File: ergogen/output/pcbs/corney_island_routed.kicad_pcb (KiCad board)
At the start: 2 copper layers, 134.2 x 92.7 mm, 67 parts

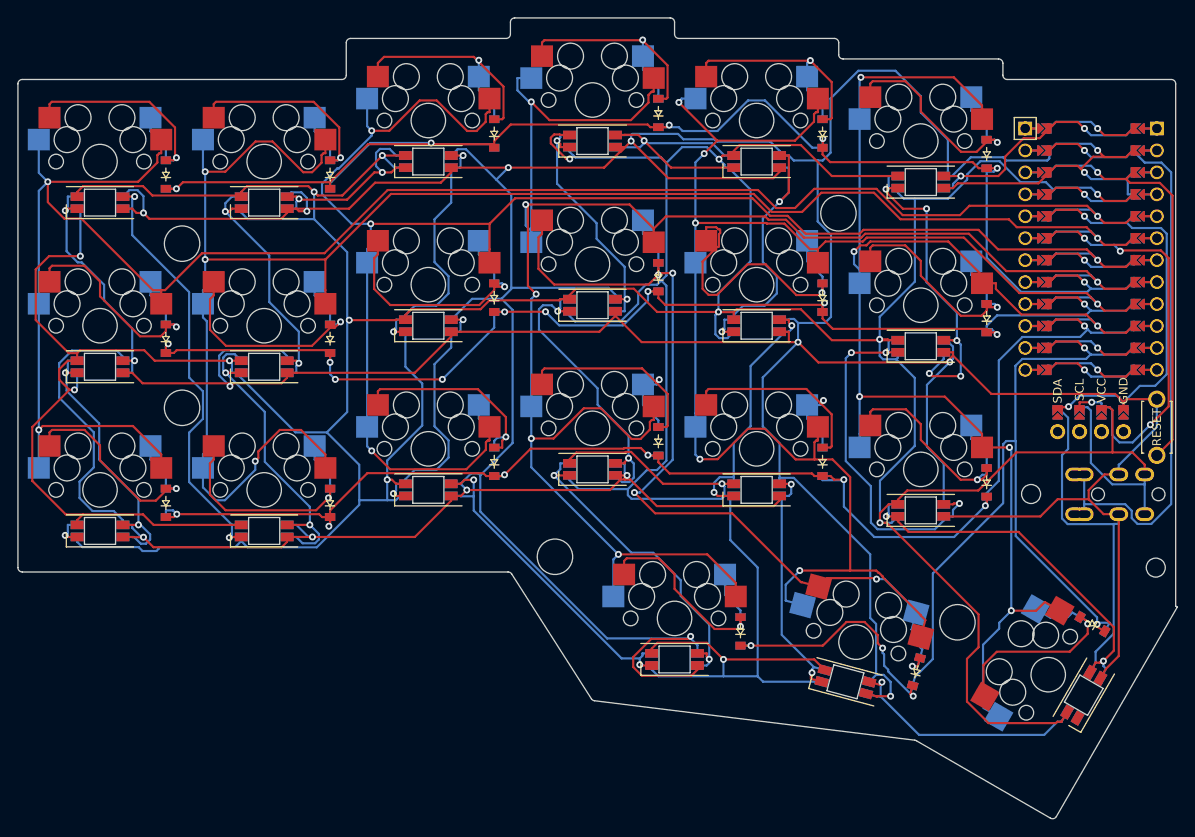
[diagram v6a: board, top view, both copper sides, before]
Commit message: Add underglow LEDs
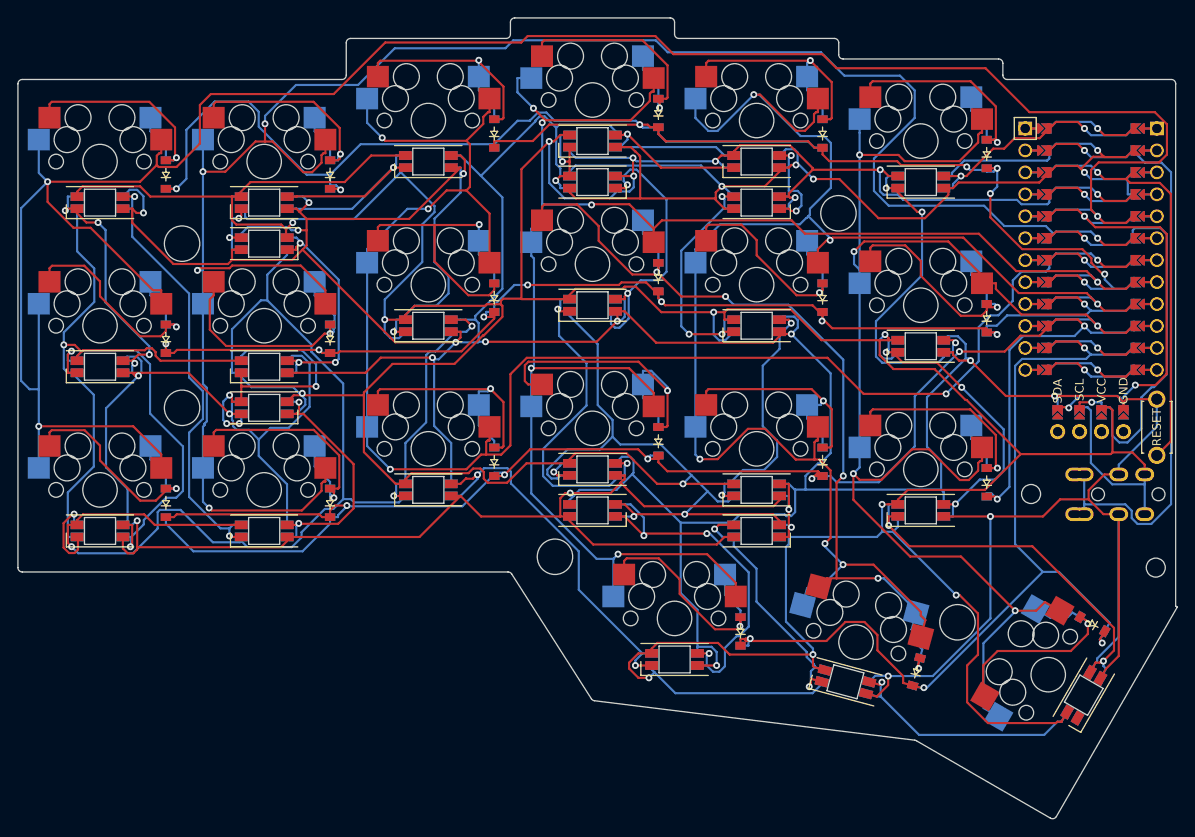
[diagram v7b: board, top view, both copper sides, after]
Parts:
- added LED23: YS-SK6812MINI-E, YS-SK6812MINI-E, F.Cu at (119.0, 71.5)
- added LED24: YS-SK6812MINI-E, YS-SK6812MINI-E, F.Cu at (157.0, 102.4)
- added LED25: YS-SK6812MINI-E, YS-SK6812MINI-E, F.Cu at (157.0, 64.4)
- added LED26: YS-SK6812MINI-E, YS-SK6812MINI-E, F.Cu at (176.0, 104.8)
- added LED27: YS-SK6812MINI-E, YS-SK6812MINI-E, F.Cu at (176.0, 66.8)
- added LED28: , combo_display, F.Cu at (214.6, 91.2)
- LED22: value combined_oled -> YS-SK6812MINI-E; footprint combined_oled -> YS-SK6812MINI-E
- moved LED22 95.6 mm to (119.0, 90.5)
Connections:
- LED10 pad 2: LED_11 -> ULED_3
- LED12 pad 2: LED_9 -> ULED_2
- LED13 pad 4: LED_5 -> ULED_5
- LED15 pad 4: LED_7 -> ULED_6
- LED22 pad 1: GND -> VCC
- LED22 pad 2: VCC -> LED_17
- LED22 pad 3: SCL -> GND
- LED22 pad 4: SDA -> ULED_0
- LED5 pad 2: LED_17 -> ULED_0
- LED6 pad 2: LED_16 -> ULED_1
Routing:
- net VCC: track 765.4 -> 879.6 mm, vias 15 -> 21
- net C0: track 222.1 -> 265.9 mm
- net R2: track 158.9 -> 193.5 mm
- net GND: track 820.9 -> 855.2 mm, vias 16 -> 23
- net ULED_0: track 0.00 -> 33.1 mm, vias 0 -> 4
- net R0: track 170.8 -> 199.7 mm, vias 6 -> 8
- net C1: track 209.1 -> 230.4 mm, vias 4 -> 5
- net ULED_6: track 0.00 -> 14.2 mm, vias 0 -> 2
- net C3: track 214.3 -> 200.6 mm
- net LED_20: track 32.9 -> 46.6 mm
- net ULED_5: track 0.00 -> 12.7 mm, vias 0 -> 2
- net ULED_2: track 0.00 -> 12.4 mm, vias 0 -> 2
- net ULED_1: track 0.00 -> 12.0 mm, vias 0 -> 2
- net R3: track 122.1 -> 110.9 mm, vias 5 -> 4
- net index_home: track 36.1 -> 27.5 mm
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
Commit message: Update LED options and rotation
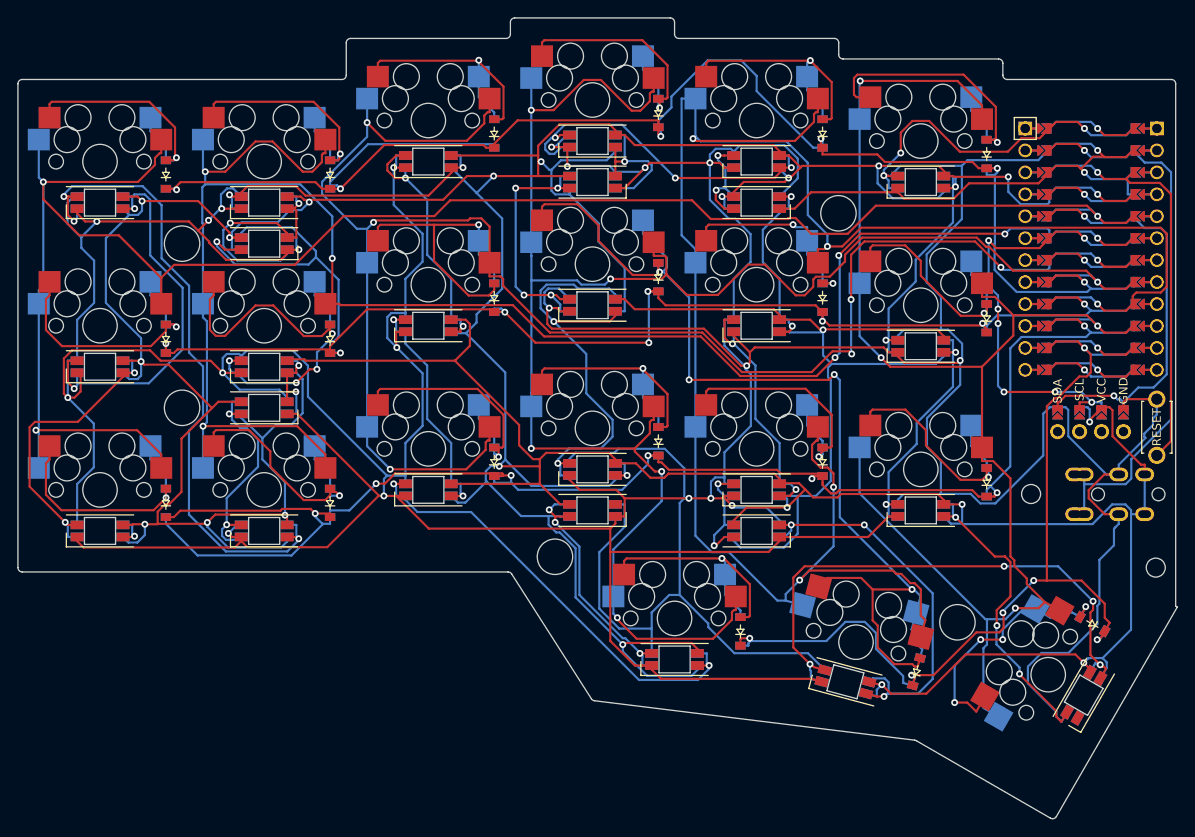
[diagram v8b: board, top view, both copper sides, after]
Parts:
- LED1, LED10, LED11, LED12, LED13, LED14, LED15, LED16, LED17, LED18, LED19, LED2, LED20, LED21, LED22, LED23, LED24, LED25, LED26, LED27, LED3, LED4, LED5, LED6, LED7, LED8, LED9: value YS-SK6812MINI-E -> (none); moved to B.Cu
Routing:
- net VCC: track 879.6 -> 789.2 mm, vias 21 -> 22
- net C0: track 265.9 -> 222.1 mm
- net GND: track 855.2 -> 897.2 mm
- net C4: track 192.3 -> 227.2 mm, vias 6 -> 5
- net LED_4: track 29.9 -> 64.7 mm, vias 1 -> 4
- net LED_16: track 27.9 -> 57.6 mm, vias 3 -> 4
- net LED_18: track 51.4 -> 77.0 mm, vias 2 -> 3
- net middle_home: track 100.7 -> 123.7 mm, vias 5 -> 4
- net ULED_0: track 33.1 -> 11.8 mm, vias 4 -> 2
- net R0: track 199.7 -> 180.2 mm, vias 8 -> 6
- net LED_5: track 30.0 -> 45.8 mm, vias 2 -> 3
- net ULED_1: track 12.0 -> 27.7 mm
- net C1: track 230.4 -> 214.9 mm, vias 5 -> 7
- net C3: track 200.6 -> 215.0 mm
- net LED_19: track 31.7 -> 45.7 mm, vias 4 -> 2
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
